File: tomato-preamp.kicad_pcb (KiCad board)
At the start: 2 copper layers, 77 x 75.6 mm, 25 parts, among them J1 IN, J2 OUT, J3.1 +ANODE, J3.2 -ANODE, J4.1 +HEATER, J4.2 -HEATER, U1 6N2P

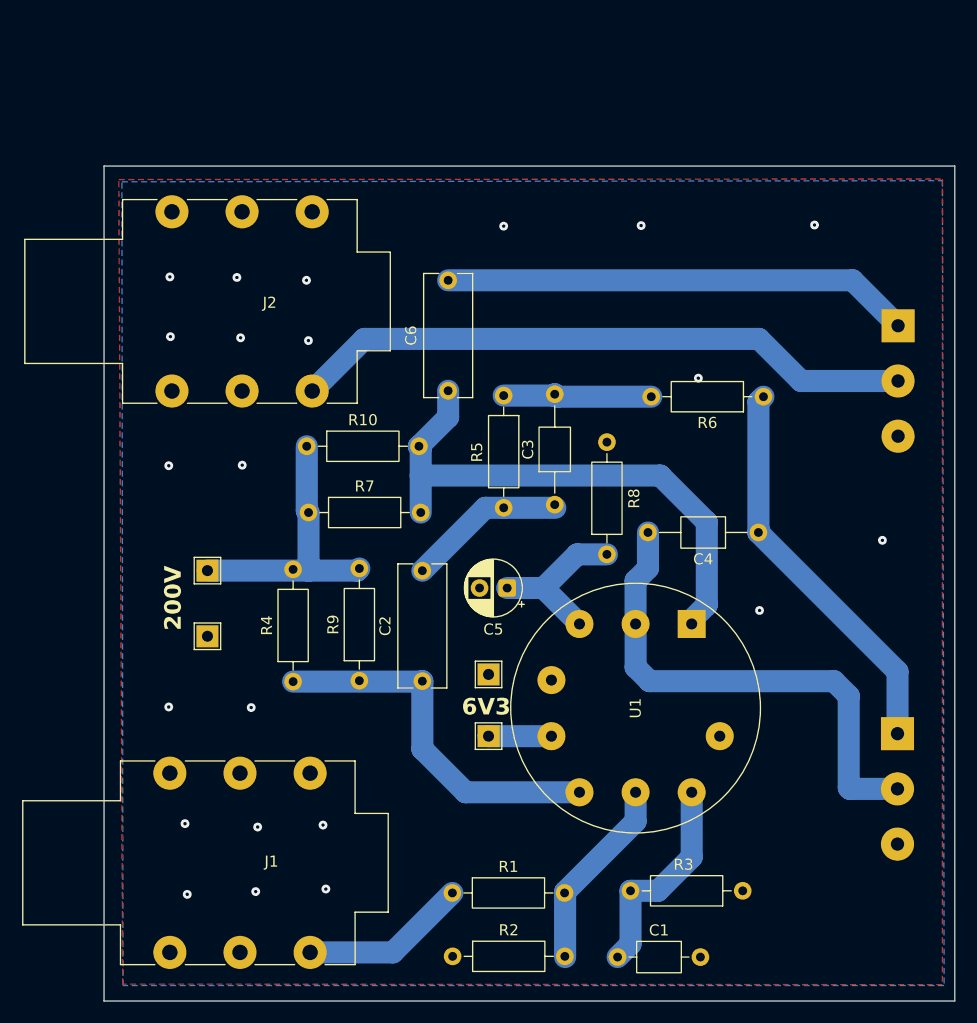
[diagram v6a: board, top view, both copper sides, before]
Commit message: Update footprints
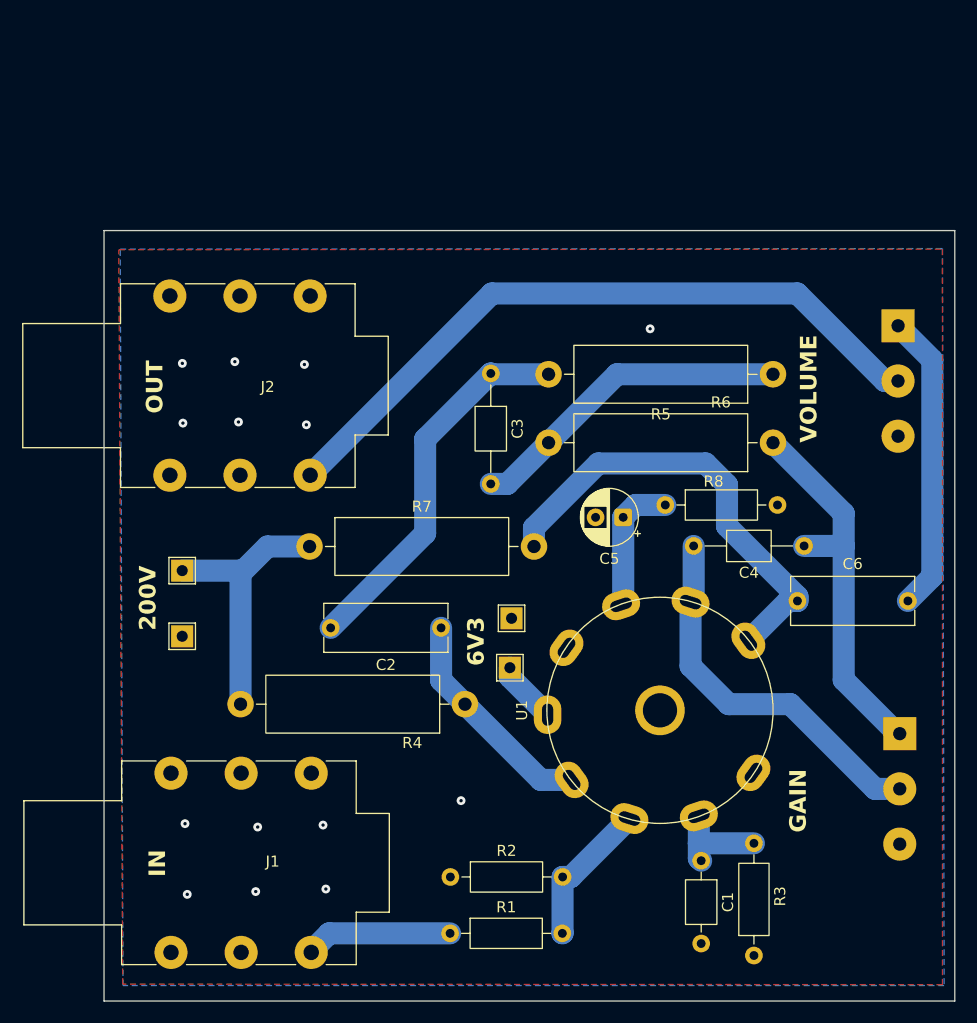
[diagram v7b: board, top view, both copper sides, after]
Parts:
- removed R10, R9: 68k, Resistor_THT:R_Axial_DIN0207_L6.3mm_D2.5mm_P10.16mm_Horizontal
- R4, R7: value 68k -> 32k; footprint Resistor_THT:R_Axial_DIN0207_L6.3mm_D2.5mm_P10.16mm_Horizontal -> Resistor_THT:R_Axial_DIN0516_L15.5mm_D5.0mm_P20.32mm_Horizontal
- R5, R6: footprint Resistor_THT:R_Axial_DIN0207_L6.3mm_D2.5mm_P10.16mm_Horizontal -> Resistor_THT:R_Axial_DIN0516_L15.5mm_D5.0mm_P20.32mm_Horizontal
- U1: footprint Valve:Valve_Noval_P -> tubes:Valve_6N2P-3
- moved C6 36.9 mm to (162.8, 95.9), turned to 0 degrees
- moved R5 24.5 mm to (160.6, 75.3), turned to 180 degrees
- moved R4 15.7 mm to (132.7, 105.2), turned to 180 degrees
- moved C3 13.2 mm to (135.0, 75.3), turned to -90 degrees
- moved C5 12.3 mm to (147.0, 88.3)
- moved C1 11.6 mm to (154.1, 119.4), turned to -90 degrees
- moved J2 7.63 mm to (118.7, 84.5)
- moved R2 7.19 mm to (131.4, 120.9)
- moved R8 6.92 mm to (150.8, 87.2), turned to 0 degrees
- moved J4.1 6.49 mm to (136.8, 101.9), turned to -90 degrees
- moved R3 5.95 mm to (158.9, 128.0), turned to 90 degrees
- moved J4.2 5.49 mm to (136.9, 97.4), turned to -90 degrees
- moved U1 5.35 mm to (158.3, 99.5)
- moved C2 5.12 mm to (130.5, 98.3), turned to 180 degrees
- moved C4 4.31 mm to (163.4, 90.9)
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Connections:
- C2 pad 1: /High voltage -> Net-(U1A-A)
- C2 pad 2: /High voltage -> Net-(C2-Pad2)
- C3 pad 1: /High voltage -> Net-(C2-Pad2)
- C4 pad 2: /High voltage -> Net-(U1B-G)
- C6 pad 1: /High voltage -> Net-(U1B-A)
- C6 pad 2: /High voltage -> Net-(C6-Pad2)
- R4 pad 1: /High voltage -> Net-(U1A-A)
- R5 pad 2: /High voltage -> Net-(C2-Pad2)
- R7 pad 2: /High voltage -> Net-(U1B-A)
- RV1 pad 2: /High voltage -> Net-(U1B-G)
- RV2 pad 1: /High voltage -> Net-(C6-Pad2)
- U1 pad 1: /High voltage -> Net-(U1B-A)
- U1 pad 2: /High voltage -> Net-(U1B-G)
- U1 pad 6: /High voltage -> Net-(U1A-A)
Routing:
- net /High voltage: track 211.2 -> 24.4 mm
- net Net-(U1B-A): track 0.00 -> 41.5 mm
- net Net-(U1B-G): track 0.00 -> 34.3 mm
- net Net-(C2-Pad2): track 0.00 -> 34.3 mm
- net Net-(C6-Pad2): track 0.00 -> 27.1 mm
- net Net-(U1A-A): track 0.00 -> 20.3 mm
- net Net-(C3-Pad2): track 13.5 -> 29.7 mm
- net Net-(U1A-K): track 19.2 -> 9.13 mm
- net Net-(J2-PadT): track 56.6 -> 63.3 mm
- net Net-(U1A-G): track 17.6 -> 13.4 mm
- net Net-(U1B-K): track 14.9 -> 12.3 mm
- net Net-(J1-PadT): track 15.1 -> 13.4 mm
- net Net-(C4-Pad1): track 36.1 -> 34.6 mm
- net GND: vias 22 -> 14
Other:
- board size 77 x 75.6 mm -> 77 x 69.8 mm
- board text added: "GAIN"
- board text added: "IN"
- board text added: "OUT"
- board text added: "VOLUME"

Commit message: Temp
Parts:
- moved R1 2.98 mm to (130.0, 123.3)
- moved R2 2.98 mm to (130.0, 118.2)
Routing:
- net GND: track 0.00 -> 253.7 mm, vias 14 -> 0
- removed copper zone on B.Cu, net GND
- removed copper zone on F.Cu, net GND
